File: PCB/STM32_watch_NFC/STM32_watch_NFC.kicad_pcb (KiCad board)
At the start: 2 copper layers, 1 part, among them U1 STM32L031G6Ux

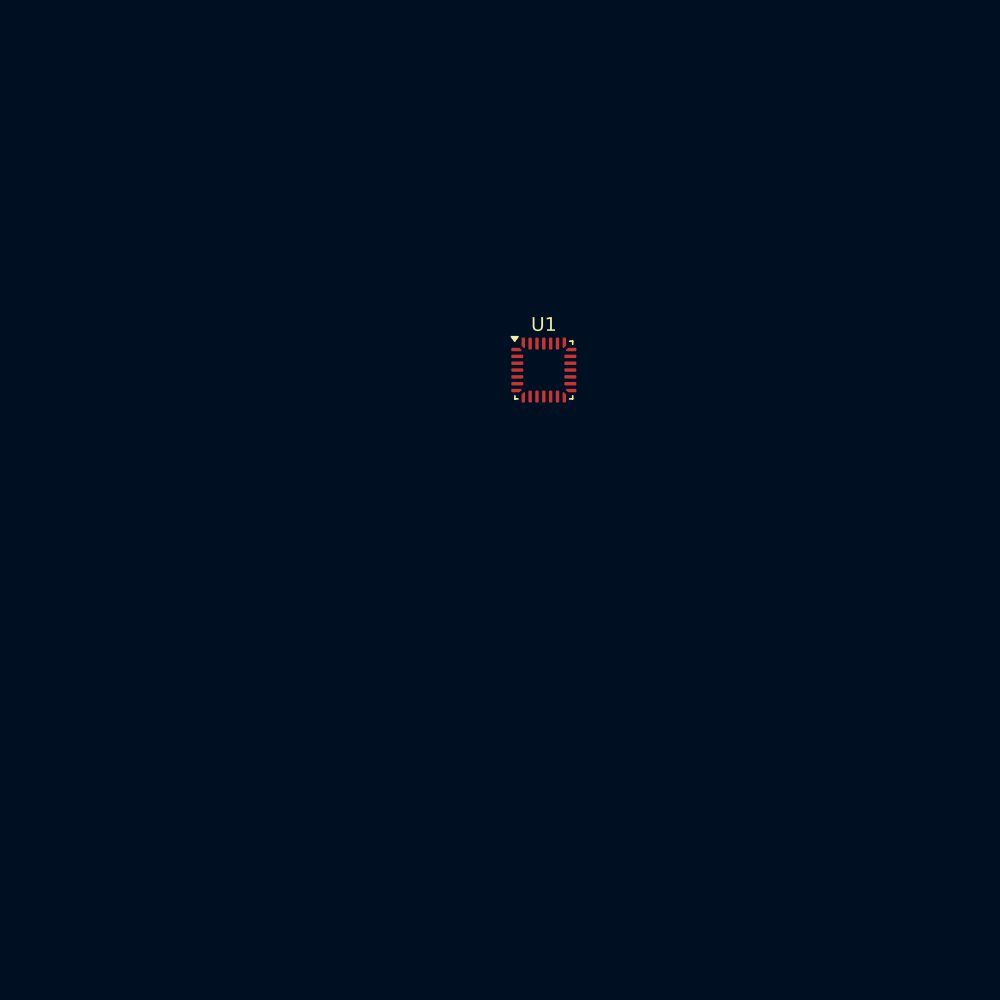
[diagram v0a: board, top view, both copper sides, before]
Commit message: Kicad - level shifter, LED, PCB layout. STM32 - PWM pin for LED
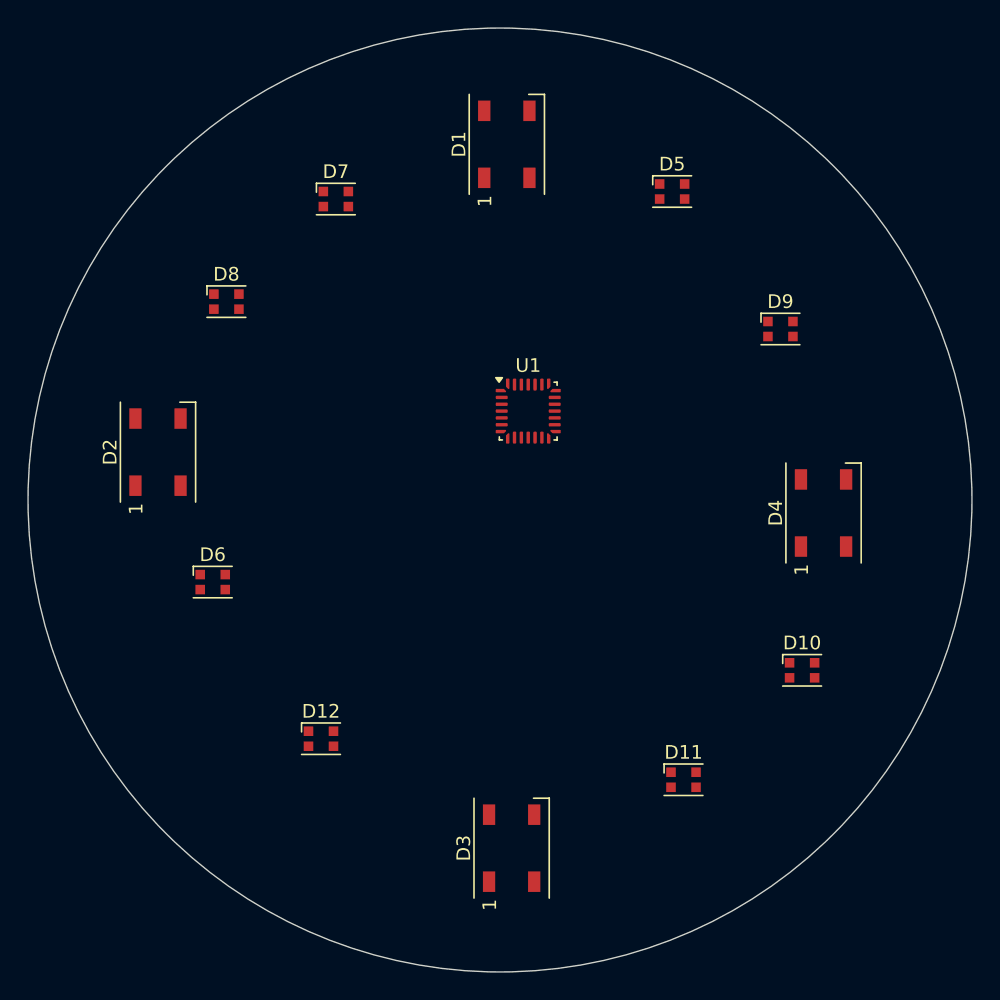
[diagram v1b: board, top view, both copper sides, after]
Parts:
- added D1: WS2812B, LED_SMD:LED_WS2812B_PLCC4_5.0x5.0mm_P3.2mm, F.Cu at (149.0, 79.0)
- added D10: WS2812B-2020, LED_SMD:LED_WS2812B-2020_PLCC4_2.0x2.0mm, F.Cu at (170.6, 117.5)
- added D11: WS2812B-2020, LED_SMD:LED_WS2812B-2020_PLCC4_2.0x2.0mm, F.Cu at (161.9, 125.5)
- added D12: WS2812B-2020, LED_SMD:LED_WS2812B-2020_PLCC4_2.0x2.0mm, F.Cu at (135.4, 122.5)
- added D2: WS2812B, LED_SMD:LED_WS2812B_PLCC4_5.0x5.0mm_P3.2mm, F.Cu at (123.5, 101.5)
- added D3: WS2812B, LED_SMD:LED_WS2812B_PLCC4_5.0x5.0mm_P3.2mm, F.Cu at (149.3, 130.4)
- added D4: WS2812B, LED_SMD:LED_WS2812B_PLCC4_5.0x5.0mm_P3.2mm, F.Cu at (172.2, 106.0)
- added D5: WS2812B-2020, LED_SMD:LED_WS2812B-2020_PLCC4_2.0x2.0mm, F.Cu at (161.1, 82.5)
- added D6: WS2812B-2020, LED_SMD:LED_WS2812B-2020_PLCC4_2.0x2.0mm, F.Cu at (127.5, 111.0)
- added D7: WS2812B-2020, LED_SMD:LED_WS2812B-2020_PLCC4_2.0x2.0mm, F.Cu at (136.5, 83.0)
- added D8: WS2812B-2020, LED_SMD:LED_WS2812B-2020_PLCC4_2.0x2.0mm, F.Cu at (128.5, 90.5)
- added D9: WS2812B-2020, LED_SMD:LED_WS2812B-2020_PLCC4_2.0x2.0mm, F.Cu at (169.0, 92.5)
- moved U1 3.21 mm to (150.6, 98.5)
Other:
- board outline added: 69 x 69 mm

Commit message: KiCad - new LEDs, STM32
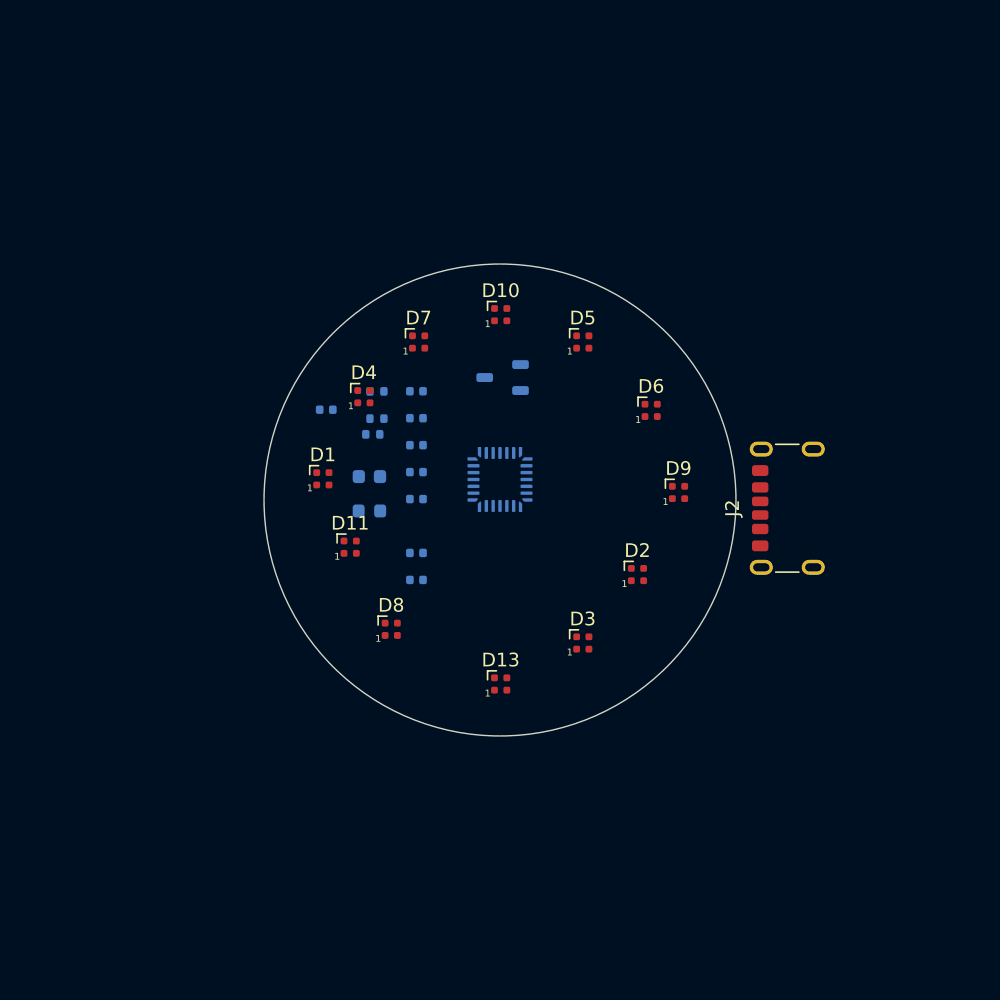
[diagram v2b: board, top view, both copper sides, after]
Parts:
- removed D12: WS2812B-2020, LED_SMD:LED_WS2812B-2020_PLCC4_2.0x2.0mm
- added C1: 100n, Capacitor_SMD:C_0402_1005Metric, B.Cu at (142.4, 97.0)
- added C2: 100n, Capacitor_SMD:C_0402_1005Metric, B.Cu at (142.4, 99.0)
- added C3: 10n, Capacitor_SMD:C_0402_1005Metric, B.Cu at (142.4, 101.0)
- added C4: 10u, Capacitor_SMD:C_0603_1608Metric, B.Cu at (139.0, 103.3)
- added C5: 1u, Capacitor_SMD:C_0402_1005Metric, B.Cu at (142.4, 103.0)
- added C6: 1u, Capacitor_SMD:C_0402_1005Metric, B.Cu at (142.4, 104.9)
- added C7: 100n, Capacitor_SMD:C_0402_1005Metric, B.Cu at (135.8, 98.4)
- added C8: 15pF, Capacitor_SMD:C_0402_1005Metric, B.Cu at (142.4, 108.9)
- added C9: 15pF, Capacitor_SMD:C_0402_1005Metric, B.Cu at (142.4, 110.8)
- added D13: SK6805, LED_SMD:LED_SK6812_EC15_1.5x1.5mm, F.Cu at (148.6, 118.5)
- added FB1: FerriteBead, Inductor_SMD:L_0603_1608Metric, B.Cu at (139.0, 105.8)
- added J2: USB_C_Receptacle_PowerOnly_6P, Connector_USB:USB_C_Receptacle_GCT_USB4125-xx-x-0190_6P_TopMnt_Horizontal, F.Cu at (170.6, 105.6)
- added Q1: 2N7000, Package_TO_SOT_SMD:TSOT-23, B.Cu at (148.7, 96.0)
- added R1: 10K, Resistor_SMD:R_0402_1005Metric, B.Cu at (139.5, 97.1)
- added R2: 10K, Resistor_SMD:R_0402_1005Metric, B.Cu at (139.5, 99.0)
- added R3: 10K, Resistor_SMD:R_0402_1005Metric, B.Cu at (139.2, 100.2)
- D1, D2, D3, D4: value WS2812B -> SK6805; footprint LED_SMD:LED_WS2812B_PLCC4_5.0x5.0mm_P3.2mm -> LED_SMD:LED_SK6812_EC15_1.5x1.5mm
- D10, D11, D5, D6, D7, D8, D9: value WS2812B-2020 -> SK6805; footprint LED_SMD:LED_WS2812B-2020_PLCC4_2.0x2.0mm -> LED_SMD:LED_SK6812_EC15_1.5x1.5mm
- U1: moved to B.Cu
- moved D2 36.2 mm to (158.6, 110.5), turned to 0 degrees
- moved D4 34.7 mm to (138.6, 97.5), turned to 0 degrees
- moved D6 34.4 mm to (159.6, 98.5)
- moved D10 34.1 mm to (148.6, 91.5)
- moved D11 29.7 mm to (137.6, 108.5)
- moved D1 27.9 mm to (135.6, 103.5), turned to 0 degrees
- moved D8 26.8 mm to (140.6, 114.5)
- moved D3 15.9 mm to (154.6, 115.5), turned to 0 degrees
- moved D9 14.1 mm to (161.6, 104.5)
- moved D5 12.8 mm to (154.6, 93.5)
- moved D7 12.1 mm to (142.6, 93.5)
- moved U1 5.41 mm to (148.5, 103.5), turned to 180 degrees
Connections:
- net Net-(U1-VSS-Pad16) renamed GND
- U1 pad 1: unconnected-(U1-VDD-Pad1) -> +3.3V
- U1 pad 17: unconnected-(U1-VDD-Pad17) -> +3.3V
- U1 pad 2: unconnected-(U1-PC14-Pad2) -> /LSE_IN
- U1 pad 21: unconnected-(U1-PA13-Pad21) -> /SWDIO
- U1 pad 22: unconnected-(U1-PA14-Pad22) -> /SWCLK
- U1 pad 27: unconnected-(U1-BOOT0-Pad27) -> Net-(U1-BOOT0)
- U1 pad 3: unconnected-(U1-PC15-Pad3) -> /LSE_OUT
- U1 pad 4: unconnected-(U1-NRST-Pad4) -> /NRST
- U1 pad 5: unconnected-(U1-VDDA-Pad5) -> +3.3VA
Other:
- board size 69 x 69 mm -> 34.5 x 34.5 mm

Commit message: Kicad, Datasheets online
Major update in PCB - new ST25R3916, LED array, bigger board, button
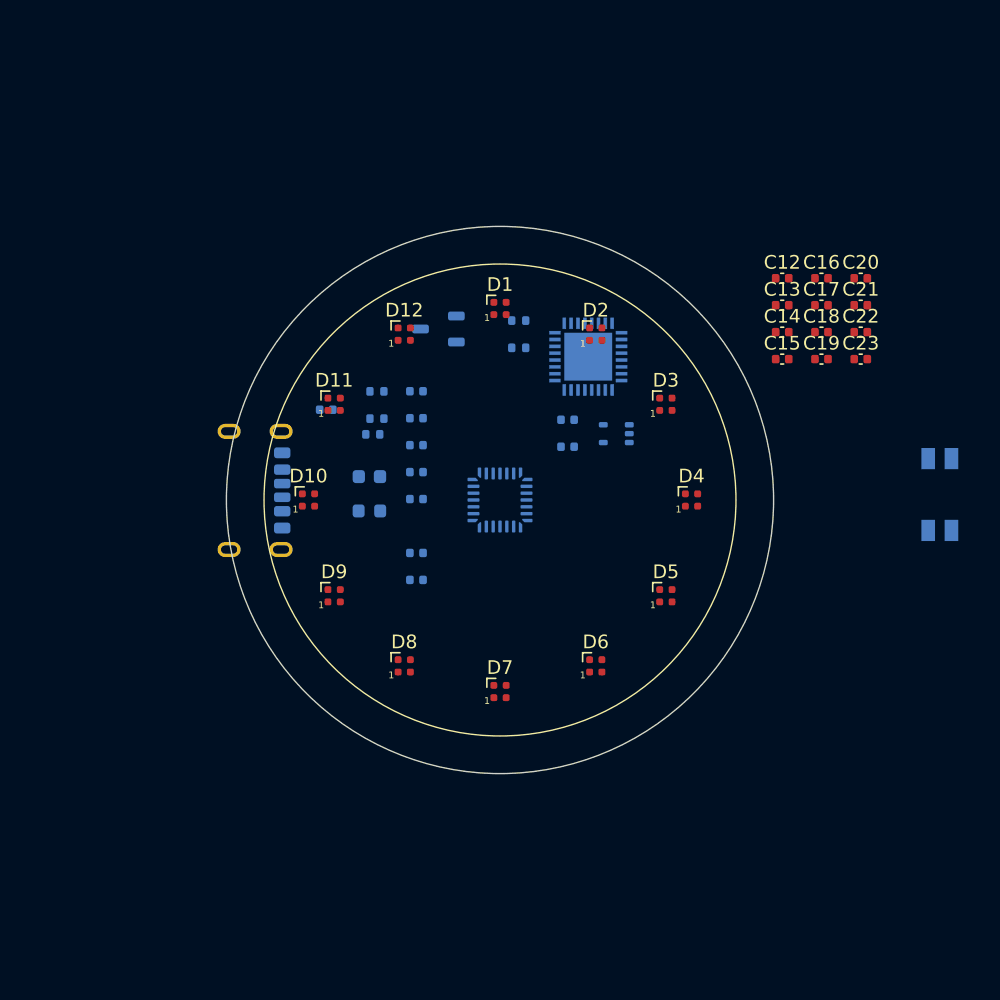
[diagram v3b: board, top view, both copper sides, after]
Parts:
- removed D13: SK6805, LED_SMD:LED_SK6812_EC15_1.5x1.5mm
- added C10: 1u, Capacitor_SMD:C_0402_1005Metric, B.Cu at (153.4, 99.1)
- added C11: 1u, Capacitor_SMD:C_0402_1005Metric, B.Cu at (153.4, 101.1)
- added C12: 100n, Capacitor_SMD:C_0402_1005Metric, F.Cu at (169.1, 88.8)
- added C13: 100n, Capacitor_SMD:C_0402_1005Metric, F.Cu at (169.1, 90.8)
- added C14: 100n, Capacitor_SMD:C_0402_1005Metric, F.Cu at (169.1, 92.7)
- added C15: 100n, Capacitor_SMD:C_0402_1005Metric, F.Cu at (169.1, 94.7)
- added C16: 100n, Capacitor_SMD:C_0402_1005Metric, F.Cu at (172.0, 88.8)
- added C17: 100n, Capacitor_SMD:C_0402_1005Metric, F.Cu at (172.0, 90.8)
- added C18: 100n, Capacitor_SMD:C_0402_1005Metric, F.Cu at (172.0, 92.7)
- added C19: 100n, Capacitor_SMD:C_0402_1005Metric, F.Cu at (172.0, 94.7)
- added C20: 100n, Capacitor_SMD:C_0402_1005Metric, F.Cu at (174.9, 88.8)
- added C21: 100n, Capacitor_SMD:C_0402_1005Metric, F.Cu at (174.9, 90.8)
- added C22: 100n, Capacitor_SMD:C_0402_1005Metric, F.Cu at (174.9, 92.7)
- added C23: 100n, Capacitor_SMD:C_0402_1005Metric, F.Cu at (174.9, 94.7)
- added D12: SK6805, LED_SMD:LED_SK6812_EC15_1.5x1.5mm, F.Cu at (141.5, 92.9)
- added R4: 5K1, Resistor_SMD:R_0402_1005Metric, B.Cu at (149.9, 91.9)
- added R5: 5K1, Resistor_SMD:R_0402_1005Metric, B.Cu at (149.9, 93.9)
- added SW1: SW_DPST_x2, Button_Switch_SMD:Panasonic_EVQPUJ_EVQPUA, B.Cu at (180.7, 104.6)
- added U2: MIC5365-3.3YC5, Package_TO_SOT_SMD:SOT-353_SC-70-5, B.Cu at (157.0, 100.2)
- added U3: ST25R3916-AQWT, ST25R3916-AQWT:QFN50P500X500X100-33N, B.Cu at (154.9, 94.5)
- J2: moved to B.Cu
- moved J2 41.1 mm to (129.5, 104.3)
- moved D9 26.3 mm to (136.4, 112.0)
- moved D7 26.2 mm to (148.5, 119.0)
- moved D4 25.1 mm to (162.5, 105.0)
- moved D10 19.5 mm to (134.5, 105.0)
- moved D5 19.5 mm to (160.6, 112.0)
- moved D6 19.1 mm to (155.5, 117.1)
- moved D3 18.5 mm to (160.6, 98.0)
- moved D1 18.0 mm to (148.5, 91.0)
- moved D2 17.8 mm to (155.5, 92.9)
- moved D11 10.5 mm to (136.4, 98.0)
- moved Q1 5.88 mm to (144.0, 92.5)
- moved D8 2.84 mm to (141.5, 117.1)
- moved U1 1.50 mm to (148.5, 105.0)
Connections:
- D1 pad 1: unconnected-(D1-DOUT-Pad1) -> Net-(D1-DOUT)
- D1 pad 2: unconnected-(D1-VSS-Pad2) -> GND
- D1 pad 3: unconnected-(D1-DIN-Pad3) -> Net-(D1-DIN)
- D1 pad 4: unconnected-(D1-VDD-Pad4) -> +5V
- D10 pad 1: unconnected-(D10-DOUT-Pad1) -> Net-(D10-DOUT)
- D10 pad 2: unconnected-(D10-VSS-Pad2) -> GND
- D10 pad 3: unconnected-(D10-DIN-Pad3) -> Net-(D10-DIN)
- D10 pad 4: unconnected-(D10-VDD-Pad4) -> +5V
- D11 pad 1: unconnected-(D11-DOUT-Pad1) -> Net-(D11-DOUT)
- D11 pad 2: unconnected-(D11-VSS-Pad2) -> GND
- D11 pad 3: unconnected-(D11-DIN-Pad3) -> Net-(D10-DOUT)
- D11 pad 4: unconnected-(D11-VDD-Pad4) -> +5V
- D2 pad 1: unconnected-(D2-DOUT-Pad1) -> Net-(D2-DOUT)
- D2 pad 2: unconnected-(D2-VSS-Pad2) -> GND
- D2 pad 3: unconnected-(D2-DIN-Pad3) -> Net-(D1-DOUT)
- D2 pad 4: unconnected-(D2-VDD-Pad4) -> +5V
- D3 pad 1: unconnected-(D3-DOUT-Pad1) -> Net-(D3-DOUT)
- D3 pad 2: unconnected-(D3-VSS-Pad2) -> GND
- D3 pad 3: unconnected-(D3-DIN-Pad3) -> Net-(D2-DOUT)
- D3 pad 4: unconnected-(D3-VDD-Pad4) -> +5V
- D4 pad 1: unconnected-(D4-DOUT-Pad1) -> Net-(D4-DOUT)
- D4 pad 2: unconnected-(D4-VSS-Pad2) -> GND
- D4 pad 3: unconnected-(D4-DIN-Pad3) -> Net-(D3-DOUT)
- D4 pad 4: unconnected-(D4-VDD-Pad4) -> +5V
- D5 pad 1: unconnected-(D5-DOUT-Pad1) -> Net-(D5-DOUT)
- D5 pad 2: unconnected-(D5-VSS-Pad2) -> GND
- D5 pad 3: unconnected-(D5-DIN-Pad3) -> Net-(D4-DOUT)
- D5 pad 4: unconnected-(D5-VDD-Pad4) -> +5V
- D6 pad 1: unconnected-(D6-DOUT-Pad1) -> Net-(D6-DOUT)
- D6 pad 2: unconnected-(D6-VSS-Pad2) -> GND
- D6 pad 3: unconnected-(D6-DIN-Pad3) -> Net-(D5-DOUT)
- D6 pad 4: unconnected-(D6-VDD-Pad4) -> +5V
- D7 pad 1: unconnected-(D7-DOUT-Pad1) -> Net-(D7-DOUT)
- D7 pad 2: unconnected-(D7-VSS-Pad2) -> GND
- D7 pad 3: unconnected-(D7-DIN-Pad3) -> Net-(D6-DOUT)
- D7 pad 4: unconnected-(D7-VDD-Pad4) -> +5V
- D8 pad 1: unconnected-(D8-DOUT-Pad1) -> Net-(D8-DOUT)
- D8 pad 2: unconnected-(D8-VSS-Pad2) -> GND
- D8 pad 3: unconnected-(D8-DIN-Pad3) -> Net-(D7-DOUT)
- D8 pad 4: unconnected-(D8-VDD-Pad4) -> +5V
- D9 pad 1: unconnected-(D9-DOUT-Pad1) -> Net-(D10-DIN)
- D9 pad 2: unconnected-(D9-VSS-Pad2) -> GND
- D9 pad 3: unconnected-(D9-DIN-Pad3) -> Net-(D8-DOUT)
- D9 pad 4: unconnected-(D9-VDD-Pad4) -> +5V
- J2 pad A12: Net-(J2-GND-PadA12) -> GND
- J2 pad A5: unconnected-(J2-CC1-PadA5) -> Net-(J2-CC1)
- J2 pad B12: Net-(J2-GND-PadA12) -> GND
- J2 pad B5: unconnected-(J2-CC2-PadB5) -> Net-(J2-CC2)
- J2 pad S1: unconnected-(J2-SHIELD-PadS1) -> GND
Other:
- board size 34.5 x 34.5 mm -> 40 x 40 mm

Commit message: Kicad
Everything about power, started to make nfc - spiral antenna problem
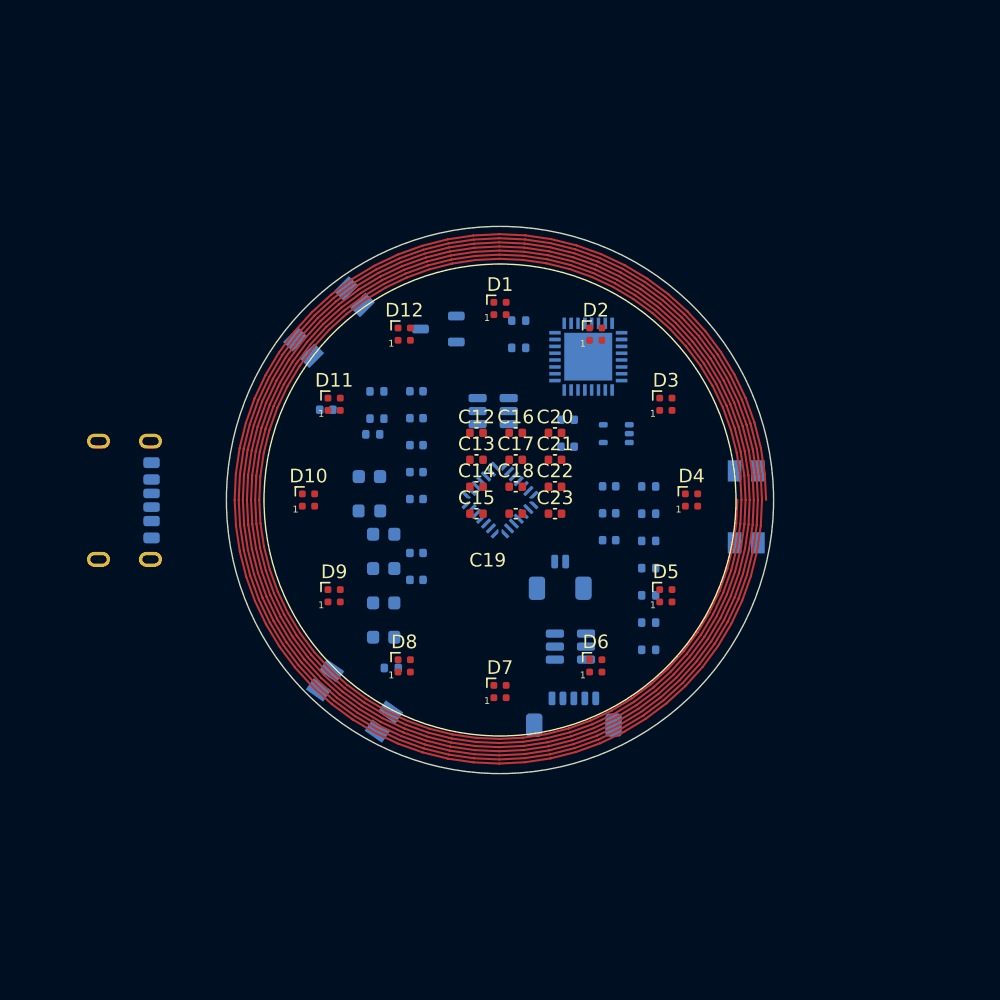
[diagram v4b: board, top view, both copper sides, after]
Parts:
- added C24: 10u, Capacitor_SMD:C_0603_1608Metric, B.Cu at (140.0, 107.5)
- added C25: 10u, Capacitor_SMD:C_0603_1608Metric, B.Cu at (140.0, 110.0)
- added C26: 22u, Capacitor_SMD:C_0603_1608Metric, B.Cu at (140.0, 112.5)
- added C27: 22u, Capacitor_SMD:C_0603_1608Metric, B.Cu at (140.0, 115.0)
- added C28: 100n, Capacitor_SMD:C_0402_1005Metric, B.Cu at (156.5, 104.0)
- added C29: 100n, Capacitor_SMD:C_0402_1005Metric, B.Cu at (156.5, 106.0)
- added C30: 100n, Capacitor_SMD:C_0402_1005Metric, B.Cu at (156.5, 107.9)
- added J1: Conn_01x06_Socket, Connector_JST:JST_SUR_SM05B-SURS-TF_1x05-1MP_P0.80mm_Horizontal, B.Cu at (153.9, 120.7)
- added Li-po1: Conn_01x02_Socket, Connector_JST:JST_SUR_SM02B-SURS-TF_1x02-1MP_P0.80mm_Horizontal, B.Cu at (152.9, 110.7)
- added ME4055A1: ~, Package_TO_SOT_SMD:SOT-23-6, B.Cu at (148.0, 98.5)
- added R10: 16.5K, Resistor_SMD:R_0402_1005Metric, B.Cu at (159.4, 106.0)
- added R11: 500, Resistor_SMD:R_0402_1005Metric, B.Cu at (159.4, 108.0)
- added R12: 16.5K, Resistor_SMD:R_0402_1005Metric, B.Cu at (159.4, 110.0)
- added R13: 500, Resistor_SMD:R_0402_1005Metric, B.Cu at (159.4, 112.0)
- added R14: 16.5K, Resistor_SMD:R_0402_1005Metric, B.Cu at (159.4, 114.0)
- added R15: 500, Resistor_SMD:R_0402_1005Metric, B.Cu at (159.4, 116.0)
- added R6: 500, Resistor_SMD:R_0402_1005Metric, B.Cu at (159.4, 104.0)
- added R7: 5K1, Resistor_SMD:R_0402_1005Metric, B.Cu at (140.6, 117.3)
- added SW2: SW_DPST_x2, Button_Switch_SMD:Panasonic_EVQPUJ_EVQPUA, B.Cu at (136.0, 92.0)
- added SW3: SW_DPST_x2, Button_Switch_SMD:Panasonic_EVQPUJ_EVQPUA, B.Cu at (137.9, 119.7)
- added U4: MT3608, Package_TO_SOT_SMD:SOT-23-6, B.Cu at (153.7, 115.7)
- moved C12 25.0 mm to (146.8, 100.1)
- moved C13 25.0 mm to (146.8, 102.1)
- moved C14 25.0 mm to (146.8, 104.0)
- moved C15 25.0 mm to (146.8, 106.0)
- moved C16 25.0 mm to (149.7, 100.1)
- moved C17 25.0 mm to (149.7, 102.1)
- moved C18 25.0 mm to (149.7, 104.0)
- moved C19 25.0 mm to (149.7, 106.0)
- moved C20 25.0 mm to (152.5, 100.1)
- moved C21 25.0 mm to (152.5, 102.1)
- moved C22 25.0 mm to (152.5, 104.0)
- moved C23 25.0 mm to (152.5, 106.0)
- moved SW1 14.2 mm to (166.5, 105.5)
- moved J2 9.58 mm to (120.0, 105.0)
- turned U1 to 45 degrees
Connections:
- net Net-(J2-VBUS-PadA9) renamed VBUS
- C10 pad 2: Net-(U2-VIN) -> +5V
- SW1 pad 1: unconnected-(SW1A-A-Pad1) -> Net-(SW1A-A)
- SW1 pad 2: unconnected-(SW1A-B-Pad2) -> +3.3V
- U1 pad 15: unconnected-(U1-PB1-Pad15) -> BATT_STM
- U1 pad 18: unconnected-(U1-PA8-Pad18) -> CHRG_STM
- U1 pad 19: unconnected-(U1-PA9-Pad19) -> DONE_STM
- U1 pad 20: unconnected-(U1-PA10-Pad20) -> Button_R
- U1 pad 23: unconnected-(U1-PA15-Pad23) -> DIN_STM
- U1 pad 6: unconnected-(U1-PA0-Pad6) -> Button_LT
- U1 pad 7: unconnected-(U1-PA1-Pad7) -> Button_LB
- U2 pad 1: Net-(U2-VIN) -> +5V
- U2 pad 3: unconnected-(U2-EN-Pad3) -> +5V
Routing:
- net unconnected-(U4-NC-Pad6): track 0.00 -> 811.2 mm
